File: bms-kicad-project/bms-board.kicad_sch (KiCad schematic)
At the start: 4 parts

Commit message: feat: added buncha shit, refer to tasks 4 and 8
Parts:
- removed H1, H2, H3, H4: MountingHole, MountingHole:MountingHole_2.7mm_M2.5, symbol Mechanical:MountingHole
- added H1, H2, H3, H4, H5, H6, H7, H8: MountingHole_Pad, MountingHole:MountingHole_3.2mm_M3_Pad_Via, symbol Mechanical:MountingHole_Pad
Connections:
- new net GND: H1.1, H2.1, H3.1, H4.1, H5.1, H6.1, H7.1, H8.1
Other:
- sheet Battery Stack Monitor ports: added C10, C11, C4, C5, S10, S11, S12, S4, S5, S6; removed none
- sheet Cell Filtering and Balancing ports: added C10, C11, C4, C5, S10, S11, S12, S4, S5, S6; removed none
- note added: "->"

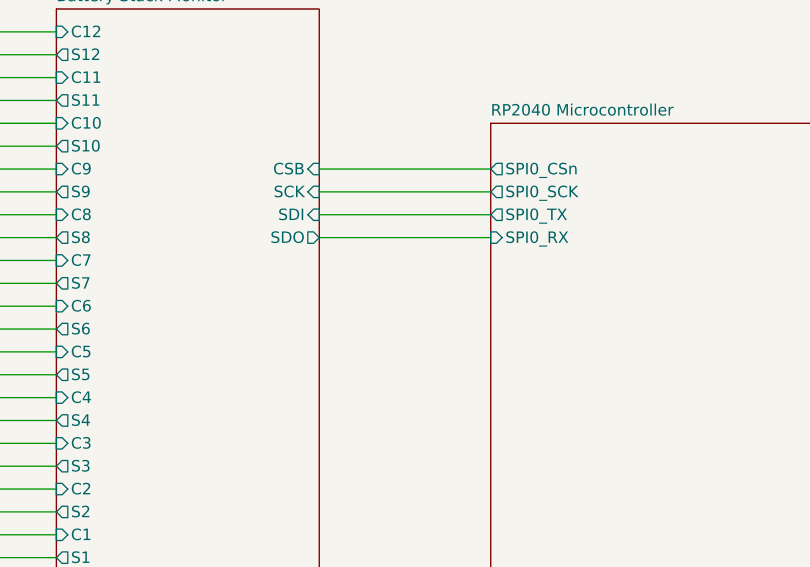
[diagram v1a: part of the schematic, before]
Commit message: feat: figured out battery stack monitor V+ biasing. Refer to task 5 on the punchlist for more details.
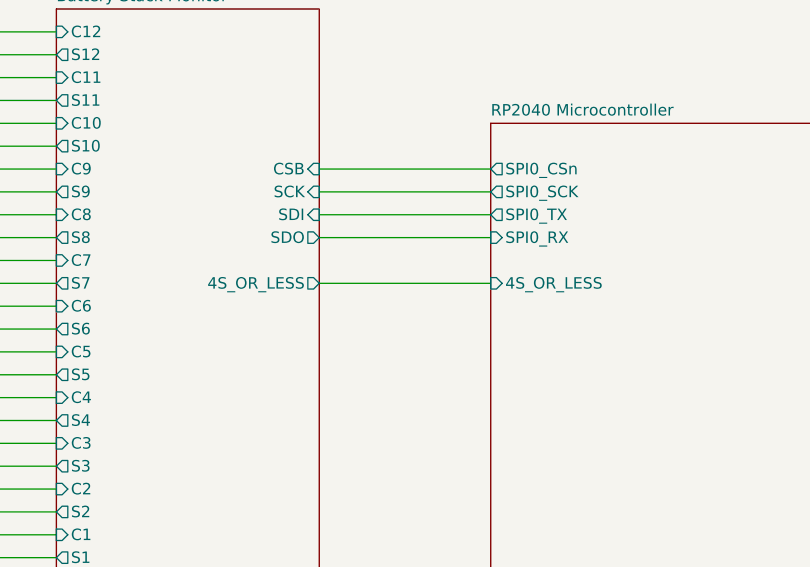
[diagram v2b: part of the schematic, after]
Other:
- sheet Battery Stack Monitor ports: added 4S_OR_LESS; removed none
- sheet RP2040 Microcontroller ports: added 4S_OR_LESS; removed none
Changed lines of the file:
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@@
+    (stroke (width 0) (type default))
+  )
+  (wire (pts (xy 146.05 87.63) (xy 165.1 87.63))
     (stroke (width 0) (type default))
   )
@@
       (effects (font (size 1.27 1.27)) (justify left))
     )
+    (pin "4S_OR_LESS" output (at 146.05 87.63 0)
+      (effects (font (size 1.27 1.27)) (justify right))
+    )
     (instances
       (project "bms-board"
@@
       (effects (font (size 1.27 1.27)) (justify left))
     )
+    (pin "4S_OR_LESS" input (at 165.1 87.63 180)
+      (effects (font (size 1.27 1.27)) (justify left))
+    )

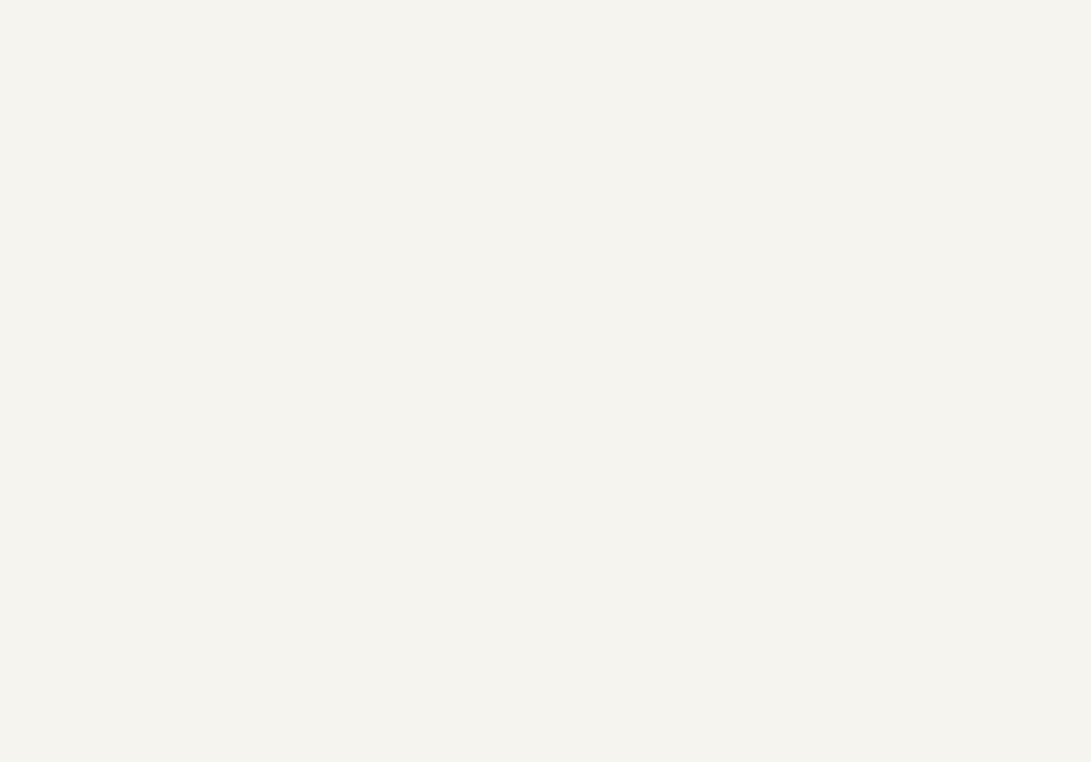
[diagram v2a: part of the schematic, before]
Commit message: feat: started a new sheet for external connections and added current sensor
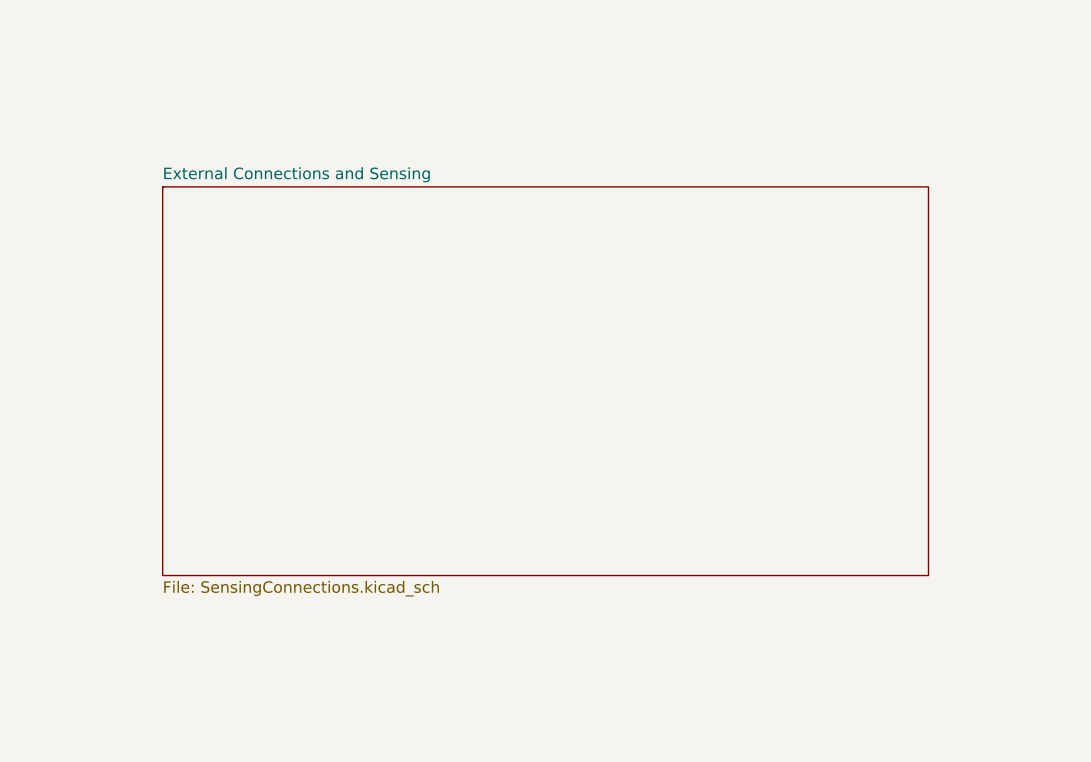
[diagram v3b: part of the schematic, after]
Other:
- added sheet External Connections and Sensing (SensingConnections.kicad_sch)
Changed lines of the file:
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@@
+    )
+  )
+  (sheet (at 116.84 147.32) (size 85.09 43.18) (fields_autoplaced)
+    (stroke (width 0.1524) (type solid))
+    (fill (color 0 0 0 0.0000))
+    (property "Sheetname" "External Connections and Sensing" (at 116.84 146.6084 0)
+      (effects (font (size 1.27 1.27)) (justify left bottom))
+    )
+    (property "Sheetfile" "SensingConnections.kicad_sch" (at 116.84 191.0846 0)
+      (effects (font (size 1.27 1.27)) (justify left top))
+    )
+    (instances
+      (project "bms-board"
+        (path "/8a7831d1-a913-4f04-8780-225d2234b41d" (page "18"))
+      )
     )
   )

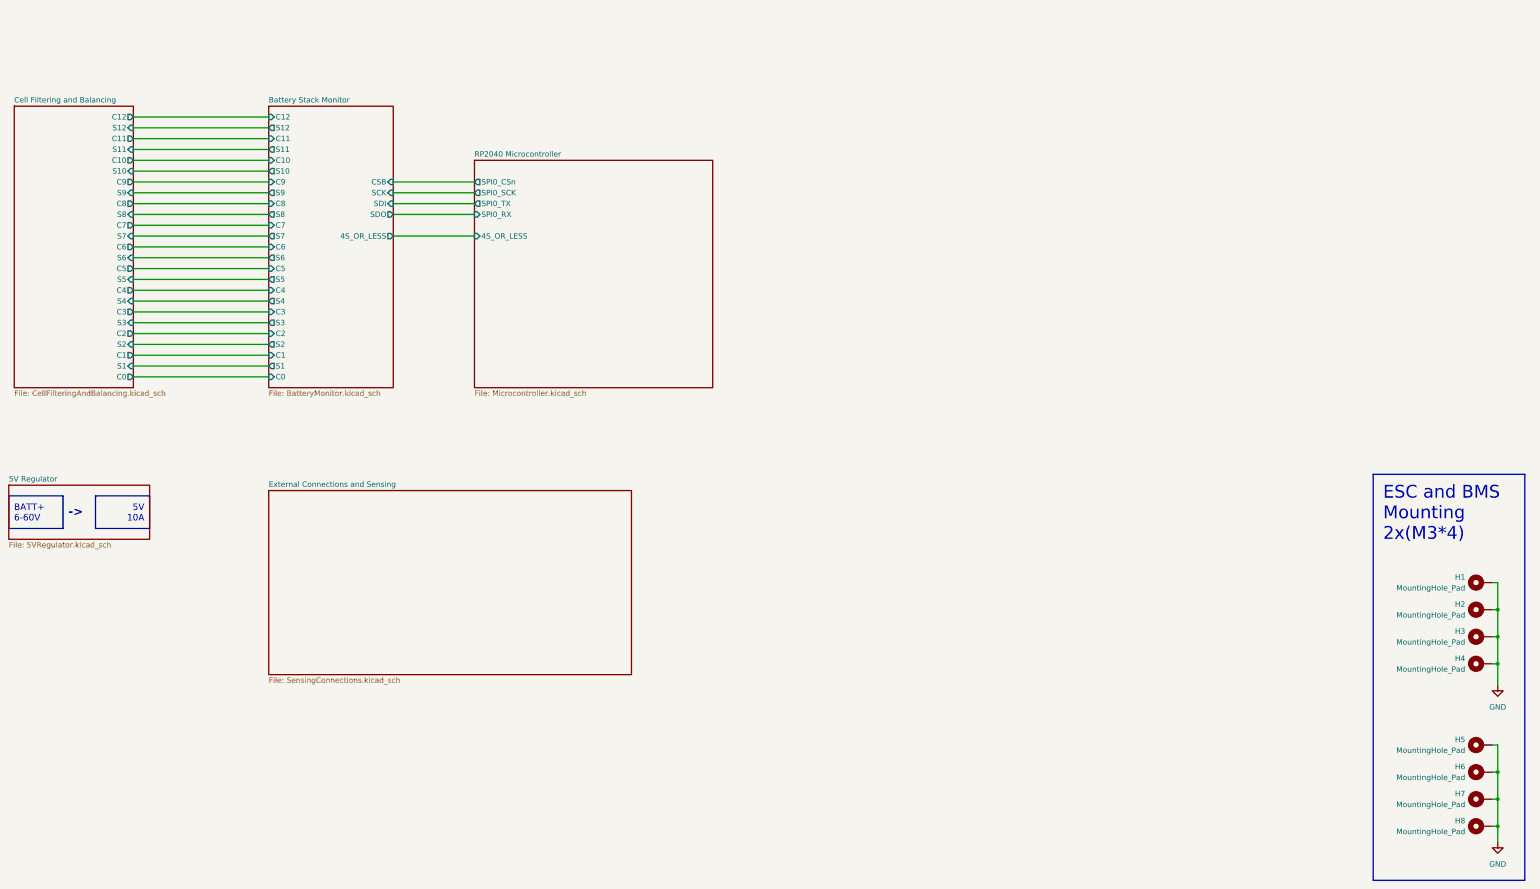
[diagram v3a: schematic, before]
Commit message: Wired up most external connections
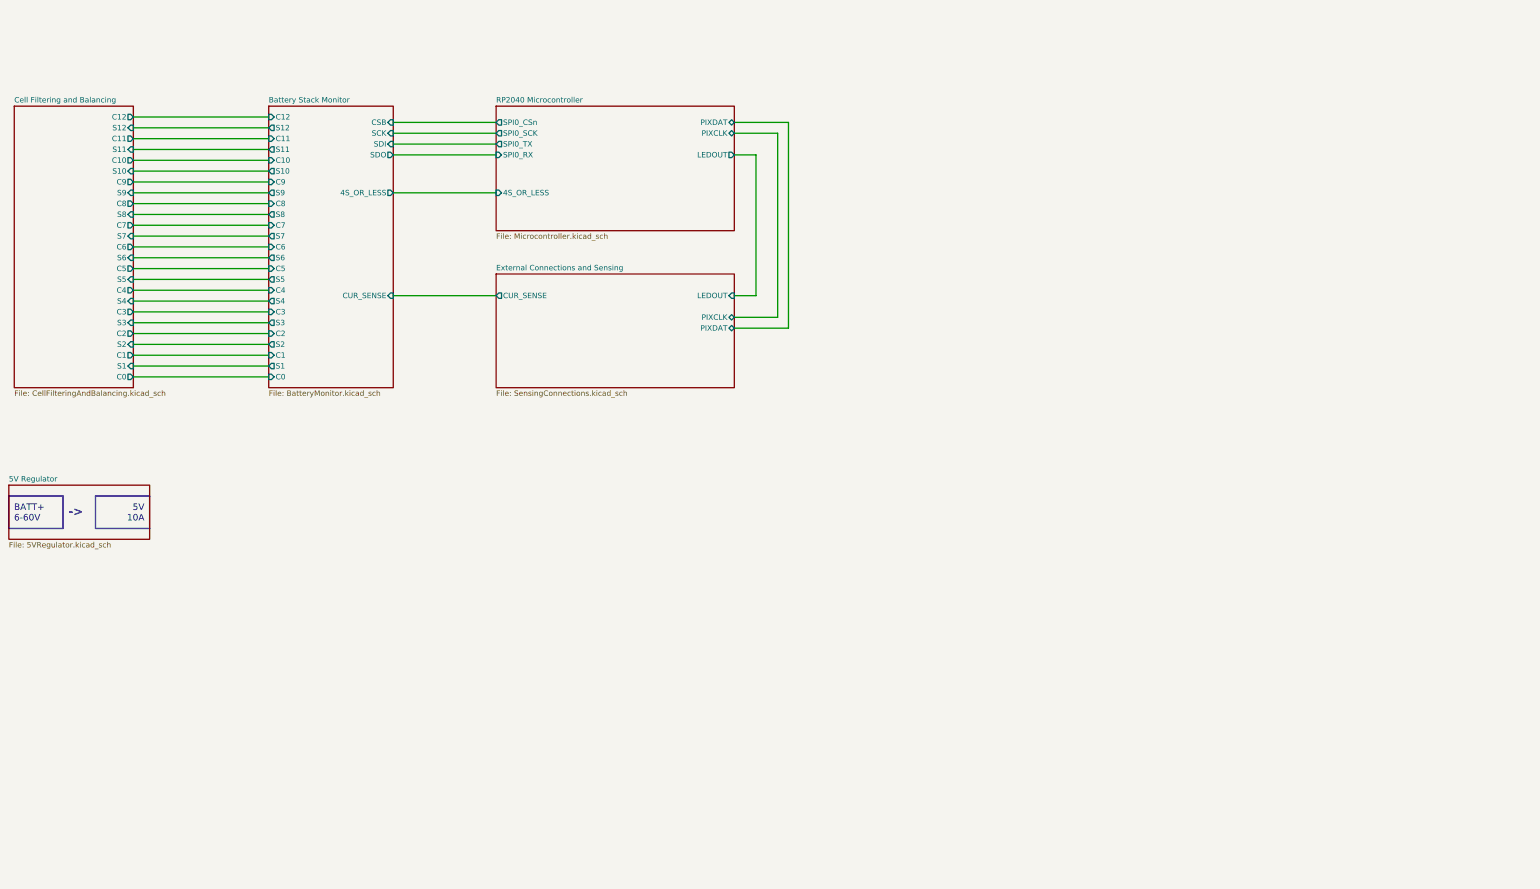
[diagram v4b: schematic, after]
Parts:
- removed H1, H2, H3, H4, H5, H6, H7, H8: MountingHole_Pad, MountingHole:MountingHole_3.2mm_M3_Pad_Via, symbol Mechanical:MountingHole_Pad
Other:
- sheet Battery Stack Monitor ports: added CUR_SENSE; removed none
- sheet External Connections and Sensing ports: added CUR_SENSE, LEDOUT, PIXCLK, PIXDAT; removed none
- sheet RP2040 Microcontroller ports: added LEDOUT, PIXCLK, PIXDAT; removed none

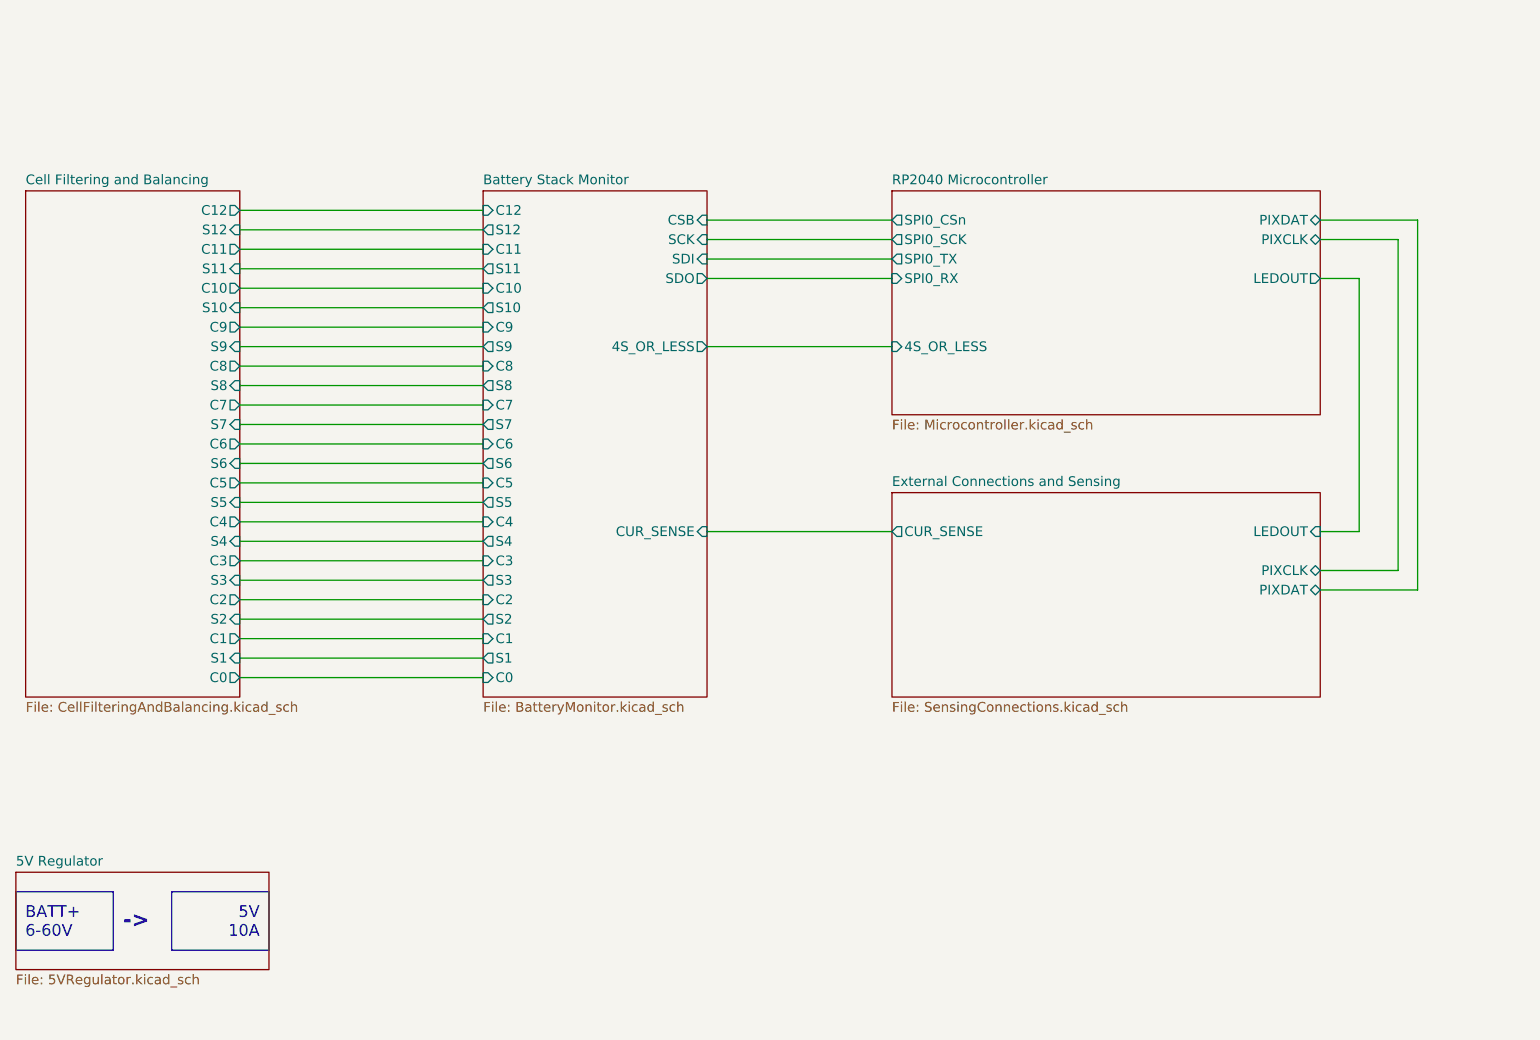
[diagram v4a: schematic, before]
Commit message: feat: cell filtering/balancing switchover done
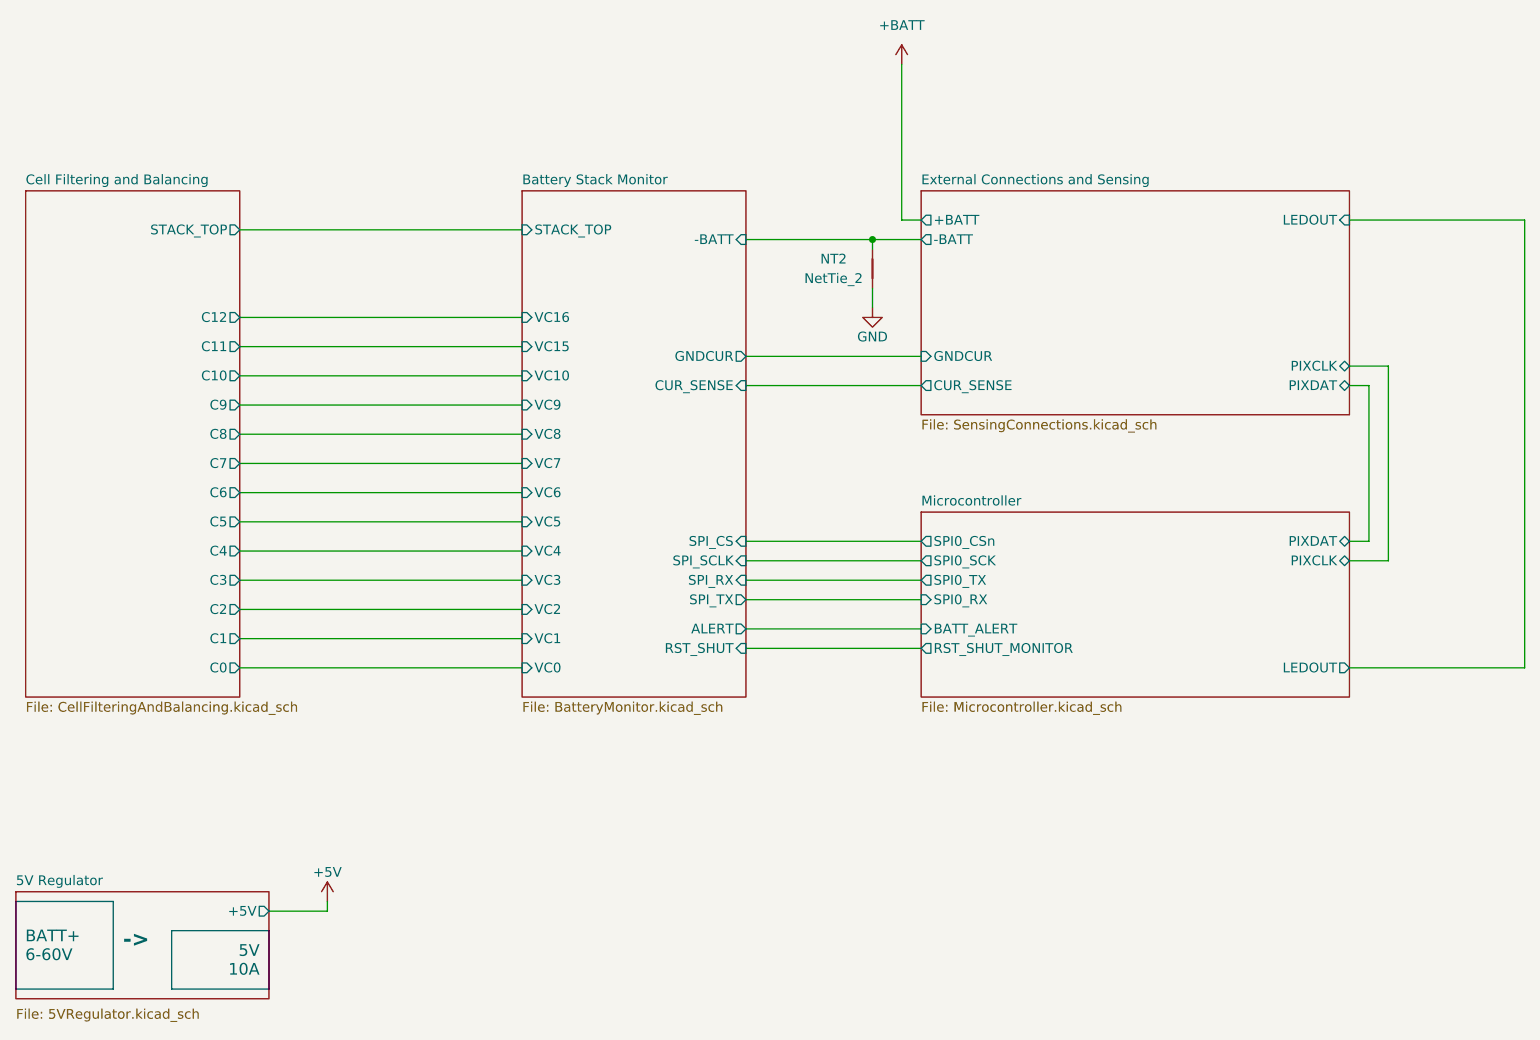
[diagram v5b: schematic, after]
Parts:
- added NT2: NetTie_2, NetTie:NetTie-2_SMD_Pad2.0mm, symbol Device:NetTie_2
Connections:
- new net Battery Stack Monitor/-BATT: NT2.2
- new net GND: NT2.1
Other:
- sheet RP2040 Microcontroller renamed Microcontroller
- sheet 5V Regulator ports: added +5V; removed none
- sheet Battery Stack Monitor ports: added -BATT, ALERT, GNDCUR, RST_SHUT, SPI_CS, SPI_RX, SPI_SCLK, SPI_TX, STACK_TOP, VC0, VC1, VC10, VC15, VC16, VC2, VC3, VC4, VC5, VC6, VC7, VC8, VC9; removed 4S_OR_LESS, C0, C1, C10, C11, C12, C2, C3, C4, C5, C6, C7, C8, C9, CSB, S1, S10, S11, S12, S2, S3, S4, S5, S6, S7, S8, S9, SCK, SDI, SDO
- sheet Cell Filtering and Balancing ports: added STACK_TOP; removed S1, S10, S11, S12, S2, S3, S4, S5, S6, S7, S8, S9
- sheet External Connections and Sensing ports: added +BATT, -BATT, GNDCUR; removed none
- sheet Microcontroller ports: added BATT_ALERT, RST_SHUT_MONITOR; removed 4S_OR_LESS

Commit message: feat: don't even know what I changed, just zoned out for several hours. Made PCB r/a mount XT-60s and solder pads into a 2-for-1 deal
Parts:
- renumbered NT2 to NT1
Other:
- sheet Battery Stack Monitor ports: added C0, C1, C10, C11, C12, C2, C3, C4, C5, C6, C7, C8, C9; removed STACK_TOP, VC0, VC1, VC10, VC15, VC16, VC2, VC3, VC4, VC5, VC6, VC7, VC8, VC9
- sheet Cell Filtering and Balancing ports: added none; removed STACK_TOP
- sheet External Connections and Sensing ports: added RGB_DIN; removed LEDOUT
- sheet Microcontroller ports: added RGB_DIN; removed LEDOUT

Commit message: feat: schematic pretty much done
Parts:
- removed NT1: NetTie_2, NetTie:NetTie-2_SMD_Pad2.0mm, symbol Device:NetTie_2
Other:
- sheet 5V Regulator ports: added none; removed +5V
- sheet External Connections and Sensing ports: added none; removed +BATT
